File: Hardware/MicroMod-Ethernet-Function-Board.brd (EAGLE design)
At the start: 38 x 65 mm, 109 parts, among them J1 MAGJACK-POE, J11 MICROMOD_STANDARD, Q1 220mA/50V/3.5Ω, Q5 20V/4.2A/52mΩ/1.4W, U1 EEPROM, U3 W5500, U4 3.3V, U5 POE_PSU-DP990X, Y1 25MHz

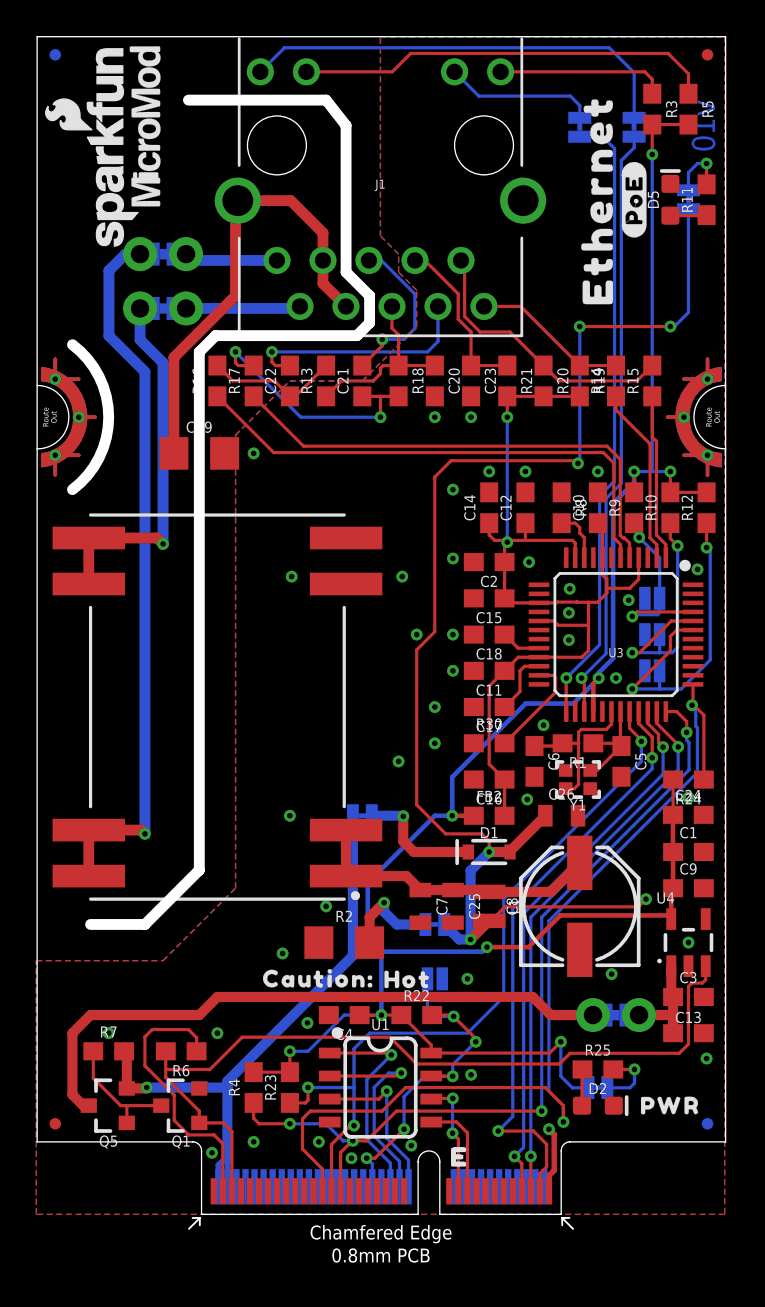
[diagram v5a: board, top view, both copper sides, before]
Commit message: Add ESD to TX/RX, landmarks to PoE module, additional GND thermals.
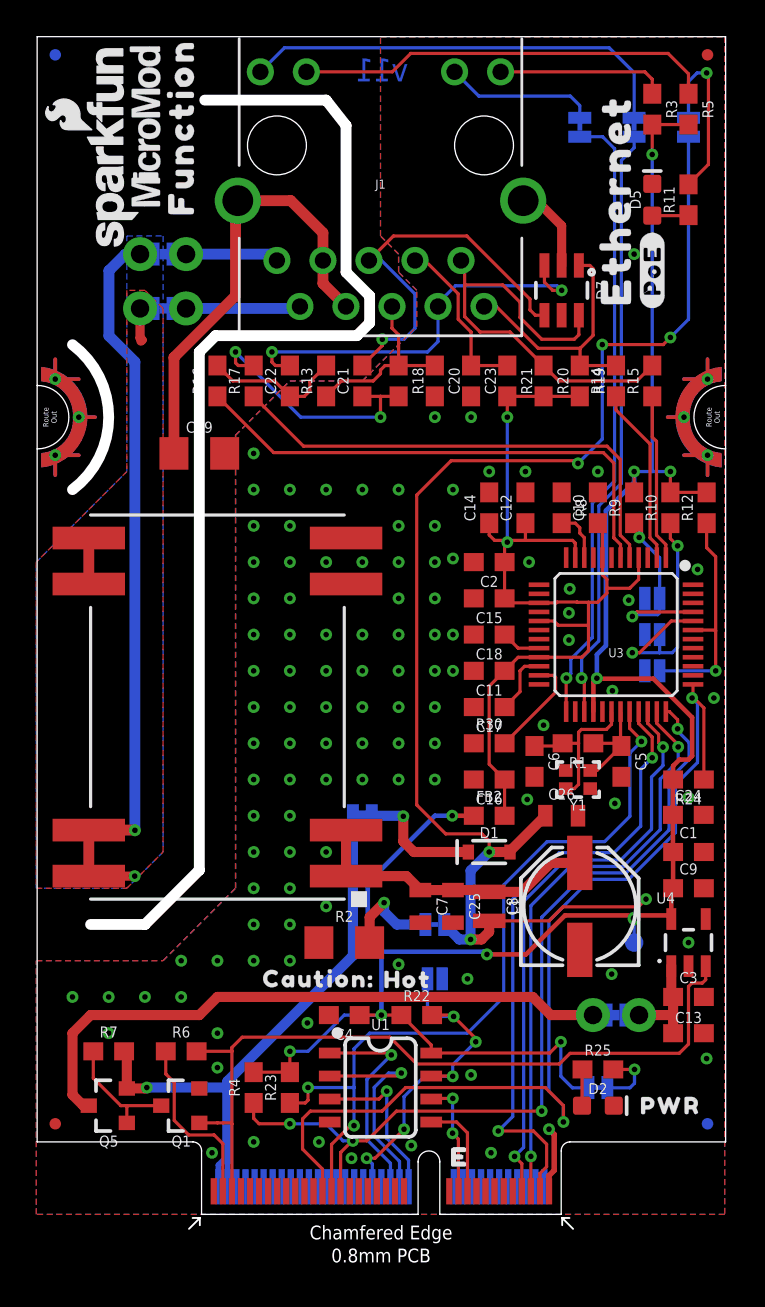
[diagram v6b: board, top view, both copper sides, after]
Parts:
- added D7: DT1042-04SO, SparkFun-DiscreteSemi:SOT-23-6
- added TP1: TEST-POINT3X4, SparkFun-Connectors:PAD.03X.04
- added U$23: (no value), output:#_POE#0
- added U$24: (no value), output:PWR1
- added U$25: (no value), output:#1
- added U$26, U$27: (no value), output:FUNCTION0
- added U$9: (no value), output:POE0
- POE: value PoE System -> (none)
- U$19: device output:#POE#0 -> output:#0
- moved LOGO3 53.5 mm to (4.00, 8.00), turned to 0 degrees
- moved U$37 9.00 mm to (18.0, 41.0)
- moved LOGO4 9.00 mm to (19.0, 42.8)
- moved U$1 7.00 mm to (18.0, 37.0)
- moved U$2 7.00 mm to (18.0, 35.0)
- moved U$18 4.03 mm to (34.0, 52.1)
- moved POE_LED 4.00 mm to (36.0, 60.0)
- moved U$19 3.61 mm to (10.0, 50.0)
- moved D5 1.00 mm to (34.0, 56.0)
- moved R11 1.00 mm to (36.0, 56.0)
- moved U$17 1.00 mm to (32.0, 56.0)
- turned R6 to 0 degrees
- renumbered JP4 to POE
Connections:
- net N$14 renamed PW1+
- net N$18 renamed PW1-
- net 3.3V: now also TP1.1
- net GND-ISO: now also D7.2
- net RD+: now also D7.3
- net RD-: now also D7.4
- net TD+: now also D7.1
- net TD-: now also D7.6
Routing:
- net PW1+: track 21.1 -> 5.18 mm, vias 1 -> 0
- net RD-: track 9.16 -> 21.6 mm
- net RD+: track 13.0 -> 22.5 mm, vias 1 -> 2
- net TD-: track 15.4 -> 24.6 mm
- net N$6: track 3.34 -> 9.85 mm
- net TD+: track 8.64 -> 14.8 mm
- net PMODE2: track 18.8 -> 12.7 mm, vias 2 -> 1
- net 3.3V_IN: track 15.1 -> 9.85 mm
- net GND-ISO: track 25.6 -> 30.5 mm
- net PWR_EN: track 45.7 -> 43.2 mm
- net ETH_!CS!: track 41.4 -> 43.3 mm
- net 5V_FILTER: track 75.0 -> 76.8 mm
- net SPI_CIPO: track 30.4 -> 32.2 mm
- net SPI_SCK: track 32.7 -> 34.5 mm
- net SPI_COPI: track 30.3 -> 32.1 mm
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- added copper zone on layer 1, net PW1+
- added copper zone on layer 16, net PW1-
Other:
- outline, holes or cut-outs redrawn
- board text added: "v11"
- board text removed: "v10"
